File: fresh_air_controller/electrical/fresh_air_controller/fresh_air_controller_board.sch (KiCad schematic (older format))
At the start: 28 parts

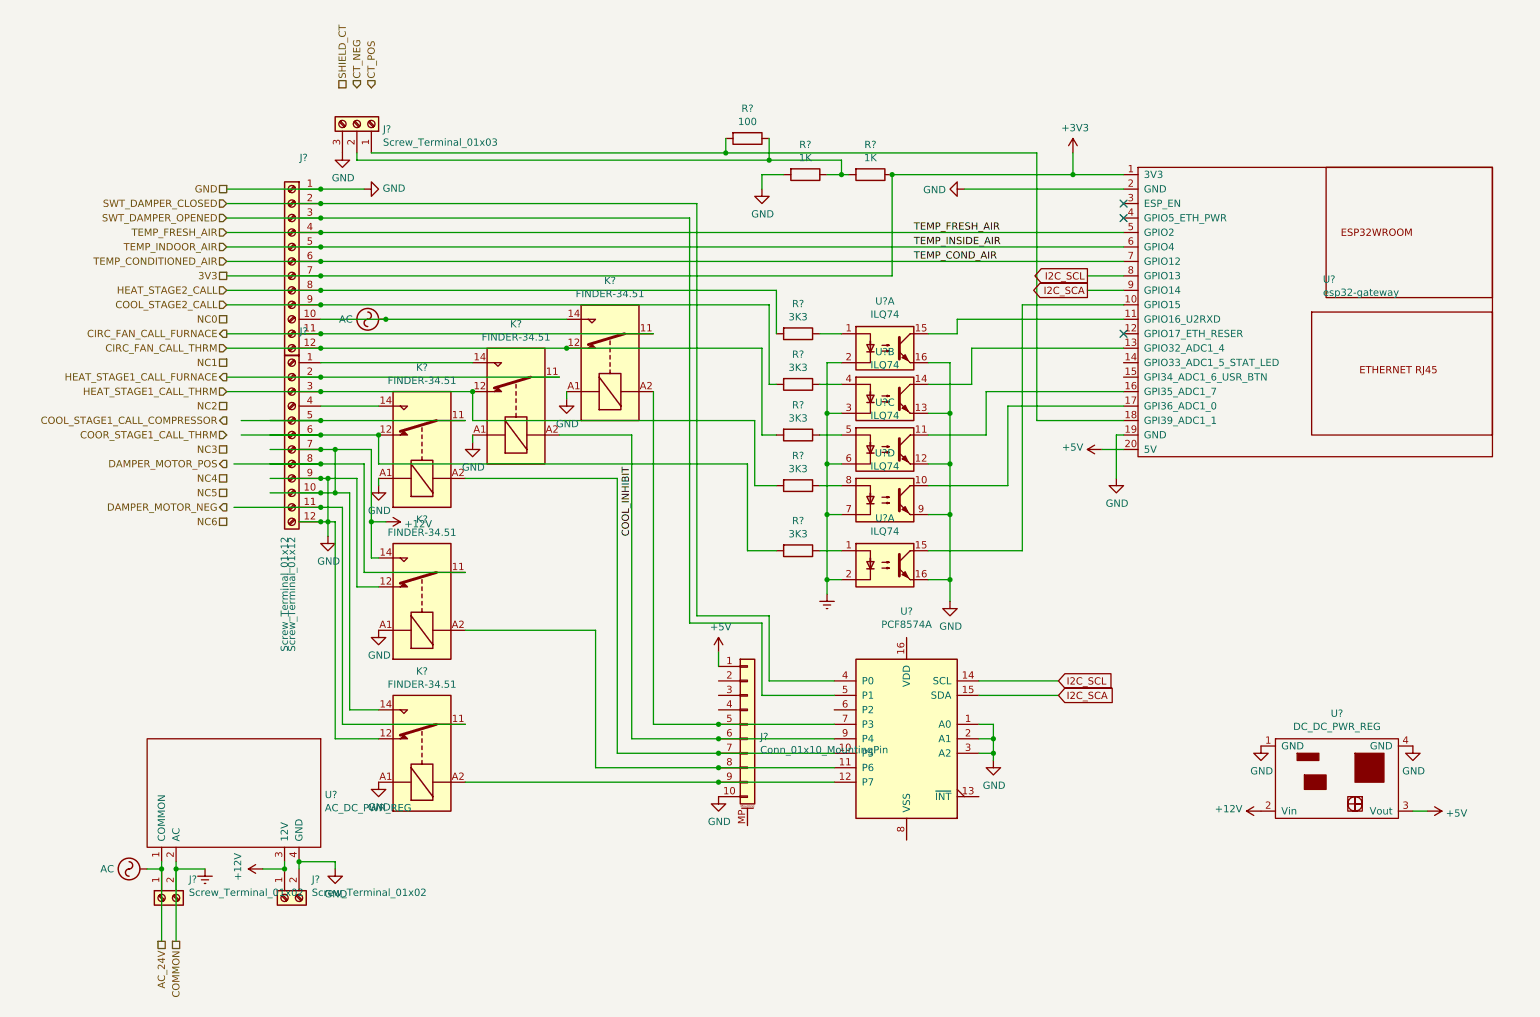
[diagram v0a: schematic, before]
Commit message: use analog_threshold for monitor and garage doors. update some pinout for fresh air controller.
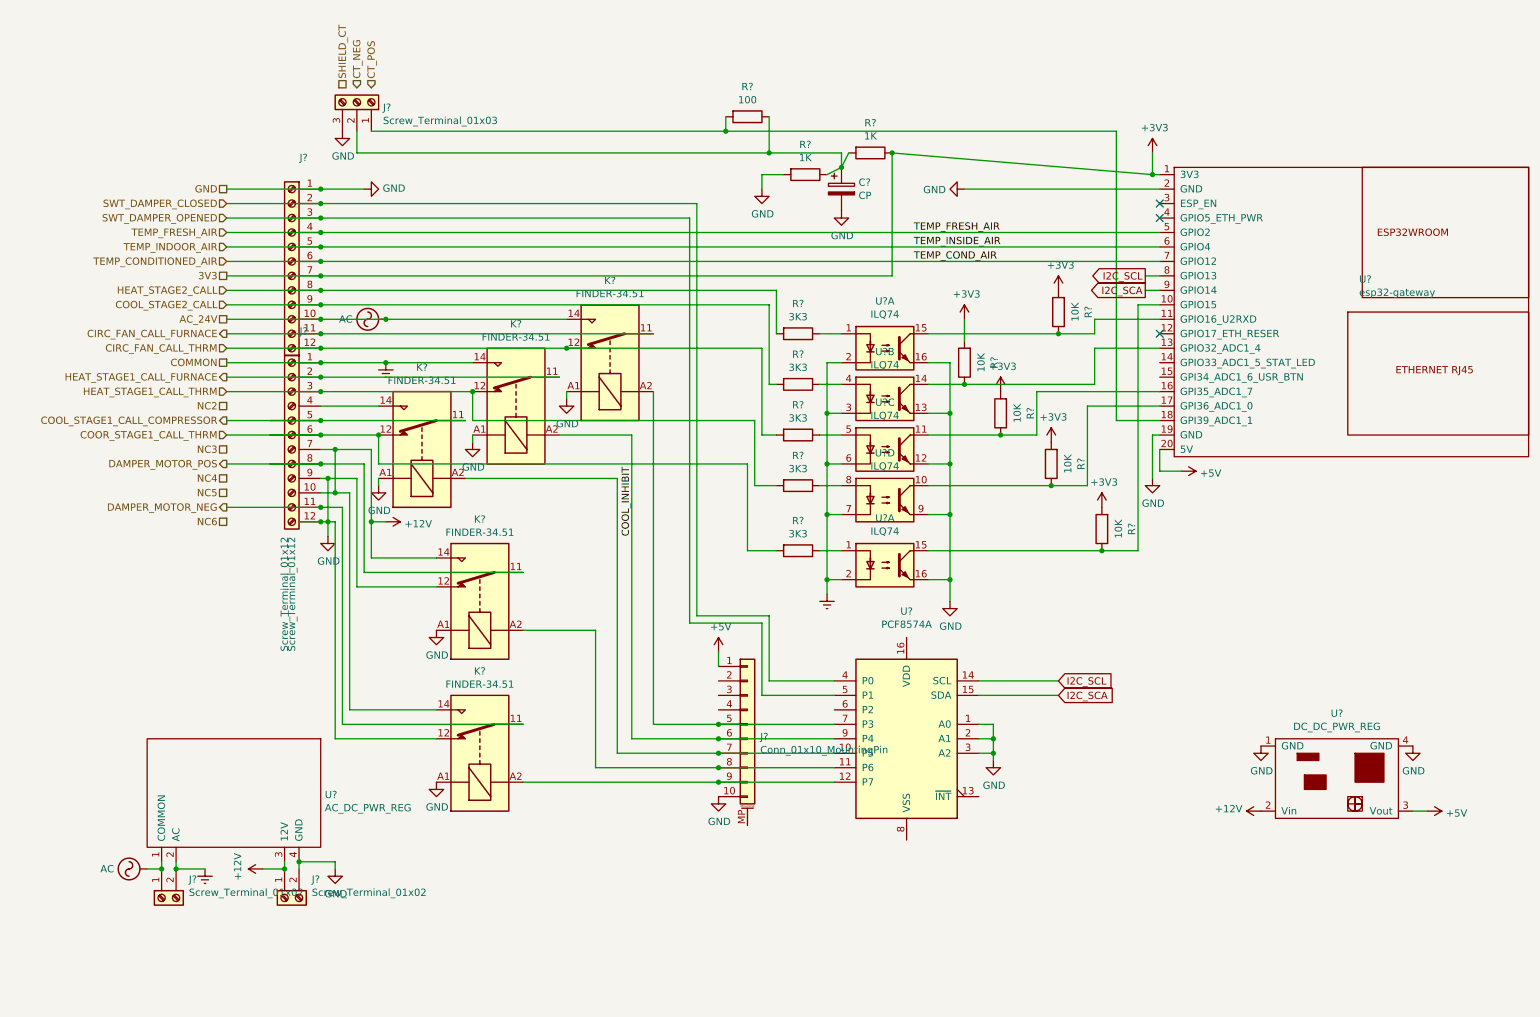
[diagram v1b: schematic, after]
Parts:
- added C?: CP, symbol Device:CP
- added R? (x5): 10K, symbol Device:R
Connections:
- net labels removed: NC0, NC1
- wire segments 197 -> 202
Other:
- moved on the sheet: J?, K?, R?, U?
